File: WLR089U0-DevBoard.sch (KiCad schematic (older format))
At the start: 24 parts, among them IC1 WLR089U0-I_RM, J1 USB_B_Micro, J2 Conn_ARM_JTAG_SWD_10, J3 Conn_01x10_Female, J4 Conn_01x10_Male, J5 Conn_01x10_Female, J6 Conn_01x02_Male, SW1 SW_Push, U1 MCP1700-3302E_SOT23, U2 CH304E

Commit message: footprint assignment done
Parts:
- C1, C2: footprint (none) -> Capacitor_SMD:C_1206_3216Metric
- C3: footprint (none) -> Capacitor_SMD:C_0603_1608Metric
- D1, D2: footprint (none) -> LED_SMD:LED_1206_3216Metric
- IC1: footprint WLR089U0IRM -> SamacSys_Parts:WLR089U0IRM
- J1: footprint (none) -> Connector_USB:USB_Micro-B_Amphenol_10103594-0001LF_Horizontal
- J2: footprint (none) -> Connector_PinHeader_1.27mm:PinHeader_2x05_P1.27mm_Vertical
- J3, J4, J5: footprint (none) -> Connector_PinHeader_1.00mm:PinHeader_1x10_P1.00mm_Vertical
- J6: footprint (none) -> Connector_PinHeader_1.00mm:PinHeader_1x02_P1.00mm_Vertical
- JP1, JP2: footprint (none) -> Jumper:SolderJumper-3_P1.3mm_Bridged12_RoundedPad1.0x1.5mm_NumberLabels
- JP3: footprint (none) -> Jumper:SolderJumper-3_P1.3mm_Open_RoundedPad1.0x1.5mm
- R1: footprint (none) -> Resistor_SMD:R_1206_3216Metric
- R2, R3: footprint (none) -> Resistor_SMD:R_0603_1608Metric
- SW1: footprint (none) -> Button_Switch_SMD:SW_Push_1P1T_NO_6x6mm_H9.5mm
- TP1, TP2, TP3: footprint (none) -> MountingHole:MountingHole_2.5mm_Pad
- U2: footprint (none) -> Package_SO:MSOP-10_3x3mm_P0.5mm
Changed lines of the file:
@@
 EESchema Schematic File Version 4
+LIBS:WLR089U0-DevBoard-cache
 EELAYER 30 0
 EELAYER END
@@
 F 0 "IC1" H 2550 3000 50  0000 C CNN
 F 1 "WLR089U0-I_RM" H 2550 2909 50  0000 C CNN
-F 2 "WLR089U0IRM" H 3100 2835 50  0001 L CNN
+F 2 "SamacSys_Parts:WLR089U0IRM" H 3100 2835 50  0001 L CNN
 F 3 "https://ww1.microchip.com/downloads/en/DeviceDoc/WLR089U0-Low-Power-LoRa-Sub-GHz-Module-Data-Sheet-DS70005435A.pdf" H 3100 2735 50  0001 L CNN
 F 4 "RF Modules Ultra-low power Long range LoRa module (863-928 MHz)" H 3100 2635 50  0001 L CNN "Description"
@@
 F 0 "C1" H 2702 1416 50  0000 L CNN
 F 1 "1u" H 2702 1325 50  0000 L CNN
-F 2 "" H 2610 1370 50  0001 C CNN
+F 2 "Capacitor_SMD:C_1206_3216Metric" H 2610 1370 50  0001 C CNN
 F 3 "~" H 2610 1370 50  0001 C CNN
 	1    2610 1370
@@
 F 0 "C2" H 4102 1426 50  0000 L CNN
 F 1 "1u" H 4102 1335 50  0000 L CNN
-F 2 "" H 4010 1380 50  0001 C CNN
+F 2 "Capacitor_SMD:C_1206_3216Metric" H 4010 1380 50  0001 C CNN
 F 3 "~" H 4010 1380 50  0001 C CNN
 	1    4010 1380
@@
 F 0 "R2" V 6720 1395 50  0000 L CNN
 F 1 "1k" V 6860 1395 50  0000 L CNN
-F 2 "" H 6790 1445 50  0001 C CNN
+F 2 "Resistor_SMD:R_0603_1608Metric" H 6790 1445 50  0001 C CNN
 F 3 "~" H 6790 1445 50  0001 C CNN
 	1    6790 1445
@@
 F 0 "D2" H 7975 1350 50  0000 R CNN
 F 1 "Green" H 8020 1530 50  0000 R CNN
-F 2 "" V 7925 1425 50  0001 C CNN
+F 2 "LED_SMD:LED_1206_3216Metric" V 7925 1425 50  0001 C CNN
 F 3 "~" V 7925 1425 50  0001 C CNN
 	1    7925 1425
@@
 F 0 "R3" V 8195 1370 50  0000 L CNN
 F 1 "1k" V 8330 1380 50  0000 L CNN
-F 2 "" H 8260 1425 50  0001 C CNN
+F 2 "Resistor_SMD:R_0603_1608Metric" H 8260 1425 50  0001 C CNN
 F 3 "~" H 8260 1425 50  0001 C CNN
 	1    8260 1425
@@
 F 0 "JP2" H 7730 3340 50  0000 C CNN
 F 1 "SolderJumper_3_Bridged12" H 7880 3604 50  0000 C CNN
-F 2 "" H 7880 3490 50  0001 C CNN
+F 2 "Jumper:SolderJumper-3_P1.3mm_Bridged12_RoundedPad1.0x1.5mm_NumberLabels" H 7880 3490 50  0001 C CNN
 F 3 "~" H 7880 3490 50  0001 C CNN
 	1    7880 3490
@@
 F 0 "C3" V 9354 3045 50  0000 C CNN
 F 1 "100n" V 9263 3045 50  0000 C CNN
-F 2 "" H 9125 3045 50  0001 C CNN
+F 2 "Capacitor_SMD:C_0603_1608Metric" H 9125 3045 50  0001 C CNN
 F 3 "~" H 9125 3045 50  0001 C CNN
 	1    9125 3045
@@
 F 0 "SW1" V 4614 3923 50  0000 L CNN
 F 1 "SW_Push" V 4705 3923 50  0000 L CNN
-F 2 "" H 4660 3975 50  0001 C CNN
+F 2 "Button_Switch_SMD:SW_Push_1P1T_NO_6x6mm_H9.5mm" H 4660 3975 50  0001 C CNN
 F 3 "~" H 4660 3975 50  0001 C CNN
 	1    4660 3775
@@
 F 0 "R1" H 4719 3421 50  0000 L CNN
 F 1 "100k" H 4719 3330 50  0000 L CNN
-F 2 "" H 4660 3375 50  0001 C CNN
+F 2 "Resistor_SMD:R_1206_3216Metric" H 4660 3375 50  0001 C CNN
 F 3 "~" H 4660 3375 50  0001 C CNN
 	1    4660 3375
@@
 F 0 "JP1" H 7735 4075 50  0000 C CNN
 F 1 "SolderJumper_3_Bridged12" H 7885 4289 50  0000 C CNN
-F 2 "" H 7885 4175 50  0001 C CNN
+F 2 "Jumper:SolderJumper-3_P1.3mm_Bridged12_RoundedPad1.0x1.5mm_NumberLabels" H 7885 4175 50  0001 C CNN
 F 3 "~" H 7885 4175 50  0001 C CNN
 	1    7885 4175
@@
 F 0 "J4" V 8855 6195 50  0000 C CNN
 F 1 "Conn_01x10_Male" V 8930 6175 50  0000 C CNN
-F 2 "" H 8995 6195 50  0001 C CNN
+F 2 "Connector_PinHeader_1.00mm:PinHeader_1x10_P1.00mm_Vertical" H 8995 6195 50  0001 C CNN
 F 3 "~" H 8995 6195 50  0001 C CNN
 	1    8995 6195
@@
 F 0 "J1" H 1075 1715 50  0000 C CNN
 F 1 "USB_B_Micro" H 1080 1625 50  0000 C CNN
-F 2 "" H 1230 1225 50  0001 C CNN
+F 2 "Connector_USB:USB_Micro-B_Amphenol_10103594-0001LF_Horizontal" H 1230 1225 50  0001 C CNN
 F 3 "~" H 1230 1225 50  0001 C CNN
 	1    1080 1275
@@
 F 0 "J2" H 1105 6605 50  0000 R CNN
 F 1 "Conn_ARM_JTAG_SWD_10" V 1165 7035 50  0000 R CNN
-F 2 "" H 1650 6585 50  0001 C CNN
+F 2 "Connector_PinHeader_1.27mm:PinHeader_2x05_P1.27mm_Vertical" H 1650 6585 50  0001 C CNN
 F 3 "http://infocenter.arm.com/help/topic/com.arm.doc.ddi0314h/DDI0314H_coresight_components_trm.pdf" V 1300 5335 50  0001 C CNN
 	1    1650 6585
@@
 F 0 "U2" H 8660 3735 50  0000 C CNN
 F 1 "CH304E" H 8755 2535 50  0000 C CNN
-F 2 "" H 8770 3740 50  0001 C CNN
+F 2 "Package_SO:MSOP-10_3x3mm_P0.5mm" H 8770 3740 50  0001 C CNN
 F 3 "" H 8770 3740 50  0001 C CNN
 	1    8870 3490
@@
 F 0 "J3" H 4483 6266 50  0000 L CNN
 F 1 "Conn_01x10_Female" V 4620 5875 50  0000 L CNN
-F 2 "" H 4455 6290 50  0001 C CNN
+F 2 "Connector_PinHeader_1.00mm:PinHeader_1x10_P1.00mm_Vertical" H 4455 6290 50  0001 C CNN
 F 3 "~" H 4455 6290 50  0001 C CNN
 	1    4455 6290
@@
 F 0 "J5" H 5403 6330 50  0000 C CNN
 F 1 "Conn_01x10_Female" V 5495 6320 50  0000 C CNN
-F 2 "" H 5330 6400 50  0001 C CNN
+F 2 "Connector_PinHeader_1.00mm:PinHeader_1x10_P1.00mm_Vertical" H 5330 6400 50  0001 C CNN
 F 3 "~" H 5330 6400 50  0001 C CNN
 	1    5330 6400
@@
 F 0 "JP3" H 8565 3135 50  0000 C CNN
 F 1 "SolderJumper_2_Open" H 8355 2950 50  0000 C CNN
-F 2 "" H 8565 3045 50  0001 C CNN
+F 2 "Jumper:SolderJumper-3_P1.3mm_Open_RoundedPad1.0x1.5mm" H 8565 3045 50  0001 C CNN
 F 3 "~" H 8565 3045 50  0001 C CNN
 	1    8565 3045
@@
 F 0 "J6" V 5220 1485 50  0000 R CNN
 F 1 "Conn_01x02_Male" V 5150 1740 50  0000 R CNN
-F 2 "" H 5275 1490 50  0001 C CNN
+F 2 "Connector_PinHeader_1.00mm:PinHeader_1x02_P1.00mm_Vertical" H 5275 1490 50  0001 C CNN
 F 3 "~" H 5275 1490 50  0001 C CNN
 	1    5275 1490
@@
 F 0 "TP1" H 9160 1515 50  0000 L CNN
 F 1 "TestPoint" H 9230 1370 50  0000 L CNN
-F 2 "" H 9425 1315 50  0001 C CNN
+F 2 "MountingHole:MountingHole_2.5mm_Pad" H 9425 1315 50  0001 C CNN
 F 3 "~" H 9425 1315 50  0001 C CNN
 	1    9225 1315
@@
 F 0 "TP3" H 10505 1515 50  0000 L CNN
 F 1 "TestPoint" H 10575 1375 50  0000 L CNN
-F 2 "" H 10765 1315 50  0001 C CNN
+F 2 "MountingHole:MountingHole_2.5mm_Pad" H 10765 1315 50  0001 C CNN
 F 3 "~" H 10765 1315 50  0001 C CNN
 	1    10565 1315
@@
 F 0 "TP2" H 9785 1515 50  0000 L CNN
 F 1 "TestPoint" H 9855 1375 50  0000 L CNN
-F 2 "" H 10050 1315 50  0001 C CNN
+F 2 "MountingHole:MountingHole_2.5mm_Pad" H 10050 1315 50  0001 C CNN
 F 3 "~" H 10050 1315 50  0001 C CNN
 	1    9850 1315
@@
 F 0 "D1" H 6591 1377 50  0000 R CNN
 F 1 "Red" H 6610 1550 50  0000 R CNN
-F 2 "" V 6545 1445 50  0001 C CNN
+F 2 "LED_SMD:LED_1206_3216Metric" V 6545 1445 50  0001 C CNN
 F 3 "~" V 6545 1445 50  0001 C CNN
 	1    6545 1445

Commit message: final footprint assignment
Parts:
- D1, D2: footprint LED_SMD:LED_1206_3216Metric -> LED_SMD:LED_0805_2012Metric
- J1: footprint Connector_USB:USB_Micro-B_Amphenol_10103594-0001LF_Horizontal -> Connector_USB:USB_Micro-AB_Molex_47590-0001
- R2, R3: footprint Resistor_SMD:R_0603_1608Metric -> Resistor_SMD:R_1206_3216Metric
- SW1: footprint Button_Switch_SMD:SW_Push_1P1T_NO_6x6mm_H9.5mm -> Button_Switch_SMD:SW_Push_SPST_NO_Alps_SKRK
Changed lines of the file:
@@
 F 0 "R2" V 6720 1395 50  0000 L CNN
 F 1 "1k" V 6860 1395 50  0000 L CNN
-F 2 "Resistor_SMD:R_0603_1608Metric" H 6790 1445 50  0001 C CNN
+F 2 "Resistor_SMD:R_1206_3216Metric" H 6790 1445 50  0001 C CNN
 F 3 "~" H 6790 1445 50  0001 C CNN
 	1    6790 1445
@@
 F 0 "D2" H 7975 1350 50  0000 R CNN
 F 1 "Green" H 8020 1530 50  0000 R CNN
-F 2 "LED_SMD:LED_1206_3216Metric" V 7925 1425 50  0001 C CNN
+F 2 "LED_SMD:LED_0805_2012Metric" V 7925 1425 50  0001 C CNN
 F 3 "~" V 7925 1425 50  0001 C CNN
 	1    7925 1425
@@
 F 0 "R3" V 8195 1370 50  0000 L CNN
 F 1 "1k" V 8330 1380 50  0000 L CNN
-F 2 "Resistor_SMD:R_0603_1608Metric" H 8260 1425 50  0001 C CNN
+F 2 "Resistor_SMD:R_1206_3216Metric" H 8260 1425 50  0001 C CNN
 F 3 "~" H 8260 1425 50  0001 C CNN
 	1    8260 1425
@@
 F 0 "SW1" V 4614 3923 50  0000 L CNN
 F 1 "SW_Push" V 4705 3923 50  0000 L CNN
-F 2 "Button_Switch_SMD:SW_Push_1P1T_NO_6x6mm_H9.5mm" H 4660 3975 50  0001 C CNN
+F 2 "Button_Switch_SMD:SW_Push_SPST_NO_Alps_SKRK" H 4660 3975 50  0001 C CNN
 F 3 "~" H 4660 3975 50  0001 C CNN
 	1    4660 3775
@@
 F 0 "J1" H 1075 1715 50  0000 C CNN
 F 1 "USB_B_Micro" H 1080 1625 50  0000 C CNN
-F 2 "Connector_USB:USB_Micro-B_Amphenol_10103594-0001LF_Horizontal" H 1230 1225 50  0001 C CNN
+F 2 "Connector_USB:USB_Micro-AB_Molex_47590-0001" H 1230 1225 50  0001 C CNN
 F 3 "~" H 1230 1225 50  0001 C CNN
 	1    1080 1275
@@
 F 0 "D1" H 6591 1377 50  0000 R CNN
 F 1 "Red" H 6610 1550 50  0000 R CNN
-F 2 "LED_SMD:LED_1206_3216Metric" V 6545 1445 50  0001 C CNN
+F 2 "LED_SMD:LED_0805_2012Metric" V 6545 1445 50  0001 C CNN
 F 3 "~" V 6545 1445 50  0001 C CNN
 	1    6545 1445

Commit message: Updated footprint assignment
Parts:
- SW1: footprint Button_Switch_SMD:SW_Push_SPST_NO_Alps_SKRK -> WLR089u0-DevBoard:Tactile Switch 3x4x2mm
- TP1, TP2, TP3: footprint MountingHole:MountingHole_2.5mm_Pad -> MountingHole:MountingHole_2.2mm_M2_DIN965_Pad_TopBottom
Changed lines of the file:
@@
 EESchema Schematic File Version 4
-LIBS:WLR089U0-DevBoard-cache
 EELAYER 30 0
 EELAYER END
@@
 F 0 "SW1" V 4614 3923 50  0000 L CNN
 F 1 "SW_Push" V 4705 3923 50  0000 L CNN
-F 2 "Button_Switch_SMD:SW_Push_SPST_NO_Alps_SKRK" H 4660 3975 50  0001 C CNN
+F 2 "WLR089u0-DevBoard:Tactile Switch 3x4x2mm" H 4660 3975 50  0001 C CNN
 F 3 "~" H 4660 3975 50  0001 C CNN
 	1    4660 3775
@@
 F 0 "TP1" H 9160 1515 50  0000 L CNN
 F 1 "TestPoint" H 9230 1370 50  0000 L CNN
-F 2 "MountingHole:MountingHole_2.5mm_Pad" H 9425 1315 50  0001 C CNN
+F 2 "MountingHole:MountingHole_2.2mm_M2_DIN965_Pad_TopBottom" H 9425 1315 50  0001 C CNN
 F 3 "~" H 9425 1315 50  0001 C CNN
 	1    9225 1315
@@
 F 0 "TP3" H 10505 1515 50  0000 L CNN
 F 1 "TestPoint" H 10575 1375 50  0000 L CNN
-F 2 "MountingHole:MountingHole_2.5mm_Pad" H 10765 1315 50  0001 C CNN
+F 2 "MountingHole:MountingHole_2.2mm_M2_DIN965_Pad_TopBottom" H 10765 1315 50  0001 C CNN
 F 3 "~" H 10765 1315 50  0001 C CNN
 	1    10565 1315
@@
 F 0 "TP2" H 9785 1515 50  0000 L CNN
 F 1 "TestPoint" H 9855 1375 50  0000 L CNN
-F 2 "MountingHole:MountingHole_2.5mm_Pad" H 10050 1315 50  0001 C CNN
+F 2 "MountingHole:MountingHole_2.2mm_M2_DIN965_Pad_TopBottom" H 10050 1315 50  0001 C CNN
 F 3 "~" H 10050 1315 50  0001 C CNN
 	1    9850 1315

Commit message: Updated footprint assignment & attached datasheet of switch
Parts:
- C1, C2: footprint Capacitor_SMD:C_1206_3216Metric -> Capacitor_SMD:C_1206_3216Metric_Pad1.33x1.80mm_HandSolder
- C3: footprint Capacitor_SMD:C_0603_1608Metric -> Capacitor_SMD:C_1206_3216Metric_Pad1.33x1.80mm_HandSolder
- D1, D2: footprint LED_SMD:LED_0805_2012Metric -> LED_SMD:LED_0805_2012Metric_Pad1.15x1.40mm_HandSolder
- J3, J4, J5: footprint Connector_PinHeader_1.00mm:PinHeader_1x10_P1.00mm_Vertical -> Connector_PinHeader_2.54mm:PinHeader_1x10_P2.54mm_Vertical
- J6: footprint Connector_PinHeader_1.00mm:PinHeader_1x02_P1.00mm_Vertical -> Connector_PinHeader_2.54mm:PinHeader_1x02_P2.54mm_Vertical
- R1, R2, R3: footprint Resistor_SMD:R_1206_3216Metric -> Resistor_SMD:R_1206_3216Metric_Pad1.42x1.75mm_HandSolder
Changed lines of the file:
@@
 F 0 "C1" H 2702 1416 50  0000 L CNN
 F 1 "1u" H 2702 1325 50  0000 L CNN
-F 2 "Capacitor_SMD:C_1206_3216Metric" H 2610 1370 50  0001 C CNN
+F 2 "Capacitor_SMD:C_1206_3216Metric_Pad1.33x1.80mm_HandSolder" H 2610 1370 50  0001 C CNN
 F 3 "~" H 2610 1370 50  0001 C CNN
 	1    2610 1370
@@
 F 0 "C2" H 4102 1426 50  0000 L CNN
 F 1 "1u" H 4102 1335 50  0000 L CNN
-F 2 "Capacitor_SMD:C_1206_3216Metric" H 4010 1380 50  0001 C CNN
+F 2 "Capacitor_SMD:C_1206_3216Metric_Pad1.33x1.80mm_HandSolder" H 4010 1380 50  0001 C CNN
 F 3 "~" H 4010 1380 50  0001 C CNN
 	1    4010 1380
@@
 F 0 "R2" V 6720 1395 50  0000 L CNN
 F 1 "1k" V 6860 1395 50  0000 L CNN
-F 2 "Resistor_SMD:R_1206_3216Metric" H 6790 1445 50  0001 C CNN
+F 2 "Resistor_SMD:R_1206_3216Metric_Pad1.42x1.75mm_HandSolder" H 6790 1445 50  0001 C CNN
 F 3 "~" H 6790 1445 50  0001 C CNN
 	1    6790 1445
@@
 F 0 "D2" H 7975 1350 50  0000 R CNN
 F 1 "Green" H 8020 1530 50  0000 R CNN
-F 2 "LED_SMD:LED_0805_2012Metric" V 7925 1425 50  0001 C CNN
+F 2 "LED_SMD:LED_0805_2012Metric_Pad1.15x1.40mm_HandSolder" V 7925 1425 50  0001 C CNN
 F 3 "~" V 7925 1425 50  0001 C CNN
 	1    7925 1425
@@
 F 0 "R3" V 8195 1370 50  0000 L CNN
 F 1 "1k" V 8330 1380 50  0000 L CNN
-F 2 "Resistor_SMD:R_1206_3216Metric" H 8260 1425 50  0001 C CNN
+F 2 "Resistor_SMD:R_1206_3216Metric_Pad1.42x1.75mm_HandSolder" H 8260 1425 50  0001 C CNN
 F 3 "~" H 8260 1425 50  0001 C CNN
 	1    8260 1425
@@
 F 0 "C3" V 9354 3045 50  0000 C CNN
 F 1 "100n" V 9263 3045 50  0000 C CNN
-F 2 "Capacitor_SMD:C_0603_1608Metric" H 9125 3045 50  0001 C CNN
+F 2 "Capacitor_SMD:C_1206_3216Metric_Pad1.33x1.80mm_HandSolder" H 9125 3045 50  0001 C CNN
 F 3 "~" H 9125 3045 50  0001 C CNN
 	1    9125 3045
@@
 F 0 "R1" H 4719 3421 50  0000 L CNN
 F 1 "100k" H 4719 3330 50  0000 L CNN
-F 2 "Resistor_SMD:R_1206_3216Metric" H 4660 3375 50  0001 C CNN
+F 2 "Resistor_SMD:R_1206_3216Metric_Pad1.42x1.75mm_HandSolder" H 4660 3375 50  0001 C CNN
 F 3 "~" H 4660 3375 50  0001 C CNN
 	1    4660 3375
@@
 F 0 "J4" V 8855 6195 50  0000 C CNN
 F 1 "Conn_01x10_Male" V 8930 6175 50  0000 C CNN
-F 2 "Connector_PinHeader_1.00mm:PinHeader_1x10_P1.00mm_Vertical" H 8995 6195 50  0001 C CNN
+F 2 "Connector_PinHeader_2.54mm:PinHeader_1x10_P2.54mm_Vertical" H 8995 6195 50  0001 C CNN
 F 3 "~" H 8995 6195 50  0001 C CNN
 	1    8995 6195
@@
 F 0 "J3" H 4483 6266 50  0000 L CNN
 F 1 "Conn_01x10_Female" V 4620 5875 50  0000 L CNN
-F 2 "Connector_PinHeader_1.00mm:PinHeader_1x10_P1.00mm_Vertical" H 4455 6290 50  0001 C CNN
+F 2 "Connector_PinHeader_2.54mm:PinHeader_1x10_P2.54mm_Vertical" H 4455 6290 50  0001 C CNN
 F 3 "~" H 4455 6290 50  0001 C CNN
 	1    4455 6290
@@
 F 0 "J5" H 5403 6330 50  0000 C CNN
 F 1 "Conn_01x10_Female" V 5495 6320 50  0000 C CNN
-F 2 "Connector_PinHeader_1.00mm:PinHeader_1x10_P1.00mm_Vertical" H 5330 6400 50  0001 C CNN
+F 2 "Connector_PinHeader_2.54mm:PinHeader_1x10_P2.54mm_Vertical" H 5330 6400 50  0001 C CNN
 F 3 "~" H 5330 6400 50  0001 C CNN
 	1    5330 6400
@@
 F 0 "J6" V 5220 1485 50  0000 R CNN
 F 1 "Conn_01x02_Male" V 5150 1740 50  0000 R CNN
-F 2 "Connector_PinHeader_1.00mm:PinHeader_1x02_P1.00mm_Vertical" H 5275 1490 50  0001 C CNN
+F 2 "Connector_PinHeader_2.54mm:PinHeader_1x02_P2.54mm_Vertical" H 5275 1490 50  0001 C CNN
 F 3 "~" H 5275 1490 50  0001 C CNN
 	1    5275 1490
@@
 F 0 "D1" H 6591 1377 50  0000 R CNN
 F 1 "Red" H 6610 1550 50  0000 R CNN
-F 2 "LED_SMD:LED_0805_2012Metric" V 6545 1445 50  0001 C CNN
+F 2 "LED_SMD:LED_0805_2012Metric_Pad1.15x1.40mm_HandSolder" V 6545 1445 50  0001 C CNN
 F 3 "~" V 6545 1445 50  0001 C CNN
 	1    6545 1445

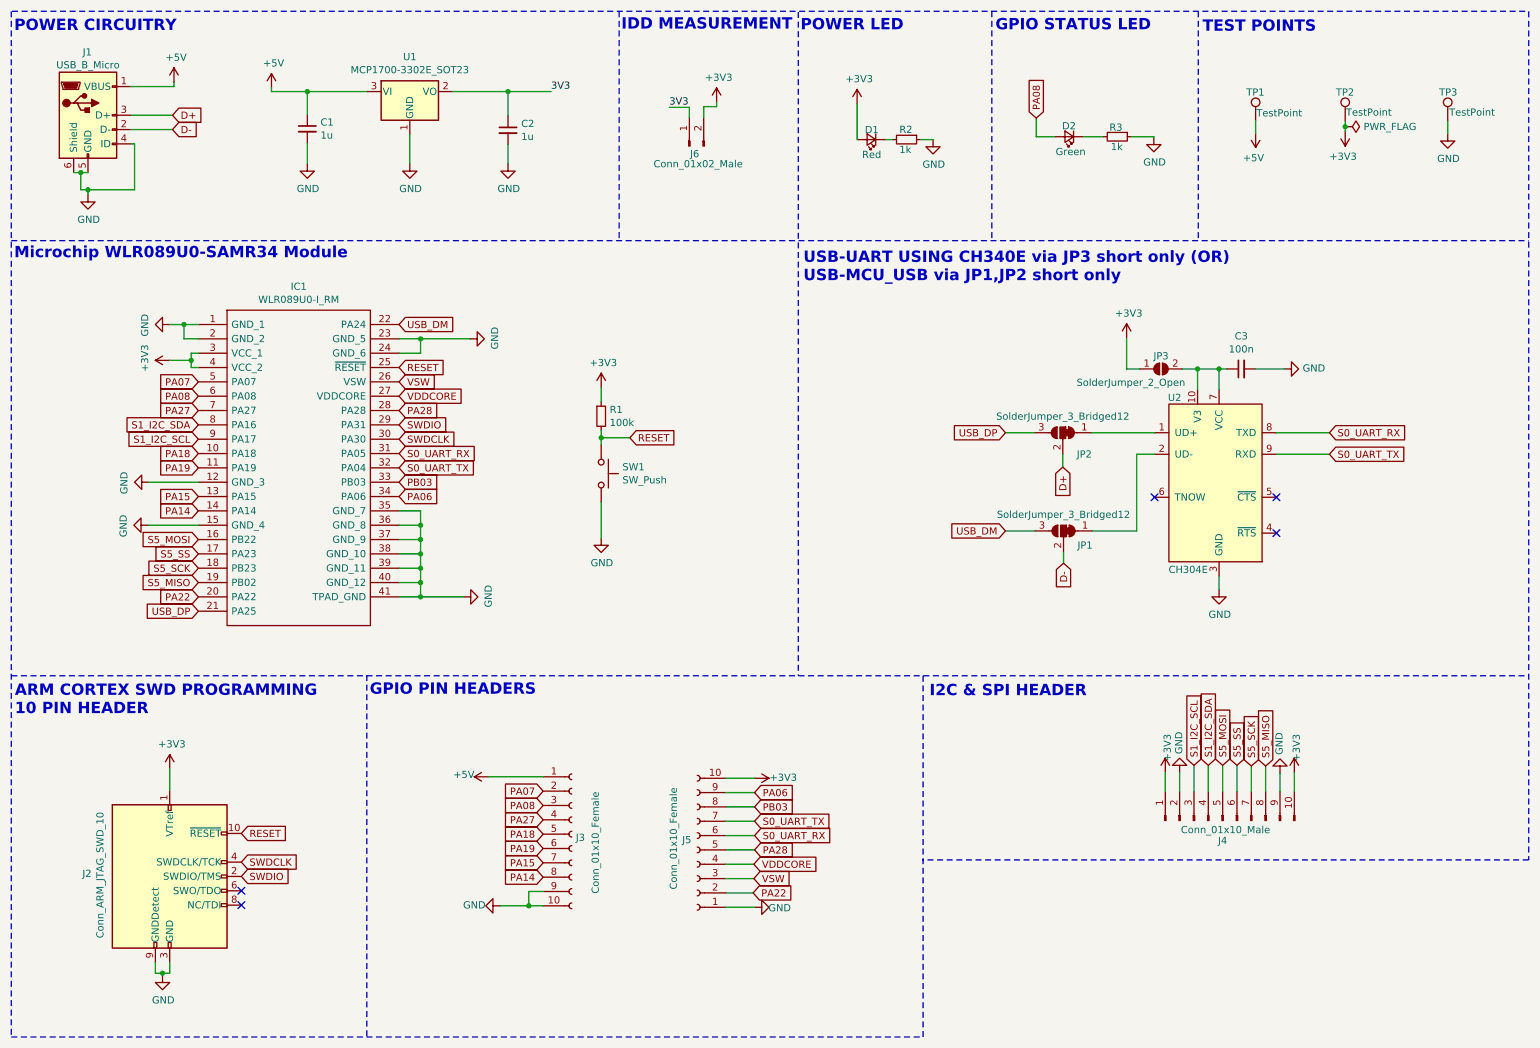
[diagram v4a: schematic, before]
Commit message: removed 5v test point, edited layout edge,microusb edge
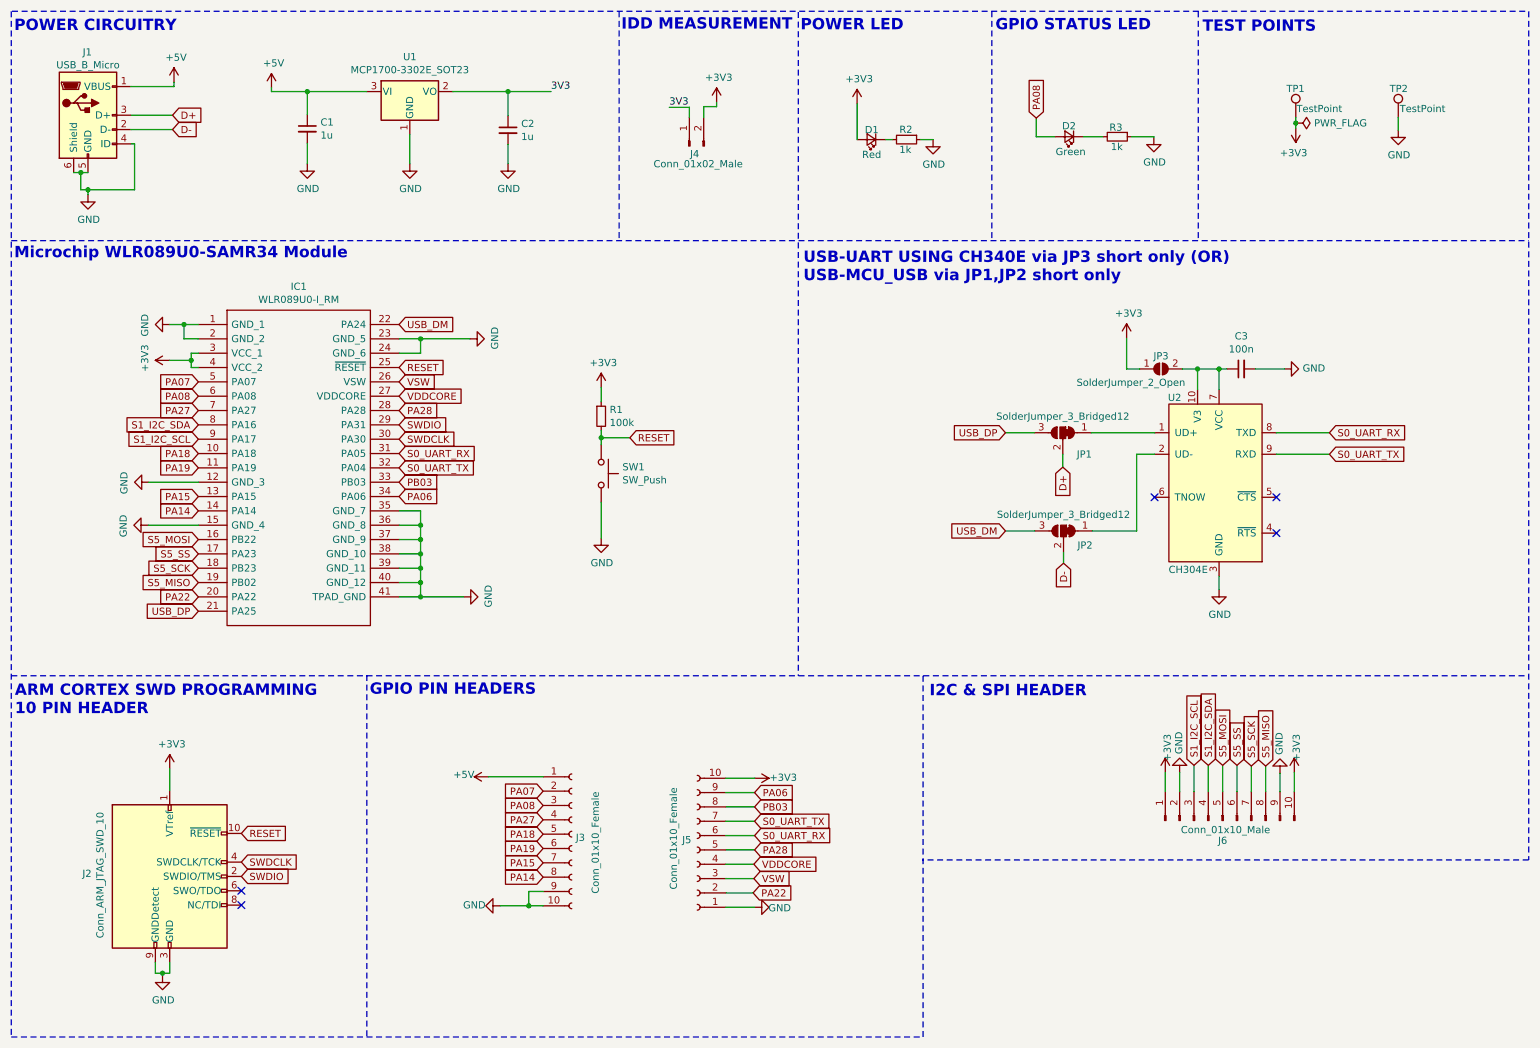
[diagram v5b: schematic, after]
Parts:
- removed TP1: TestPoint, MountingHole:MountingHole_2.2mm_M2_DIN965_Pad_TopBottom, symbol Connector:TestPoint
- renumbered J6 to J4, J4 to J6, JP2 to JP1, JP1 to JP2, TP2 to TP1, TP3 to TP2
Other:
- moved on the sheet: TP1, TP2
